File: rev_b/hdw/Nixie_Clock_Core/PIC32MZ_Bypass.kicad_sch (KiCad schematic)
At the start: 18 parts

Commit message: lots of rev B control board schematic progress
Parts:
- renumbered C1616 to C?, C1622 to C?, C1601 to C?, C1615 to C?, C1608 to C?, C1609 to C?, C1602 to C?, C1623 to C?, L1601 to L?, L1602 to L?

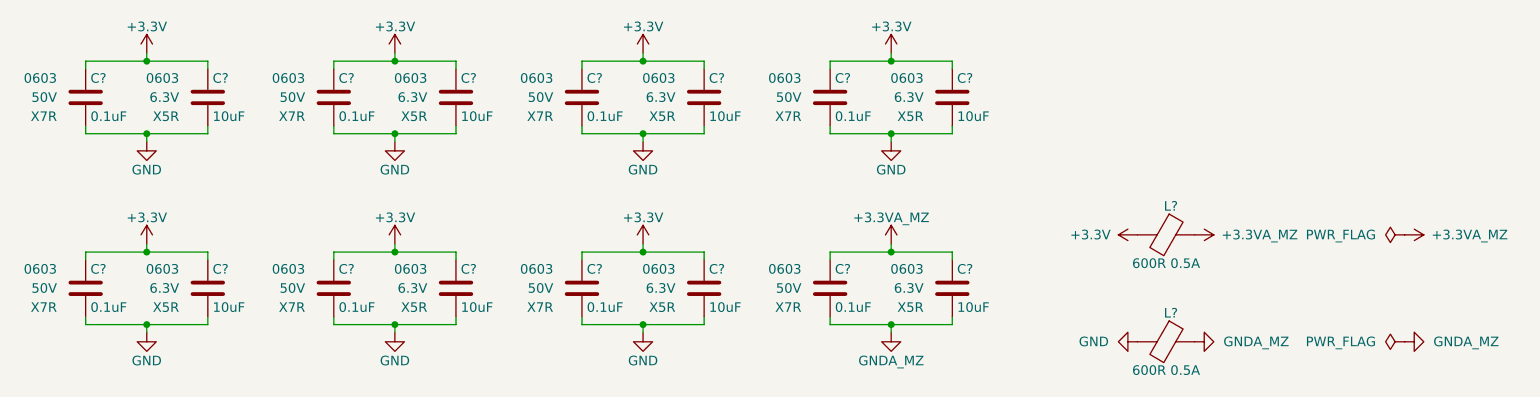
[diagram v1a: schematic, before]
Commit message: updated footprints, ran some DRC
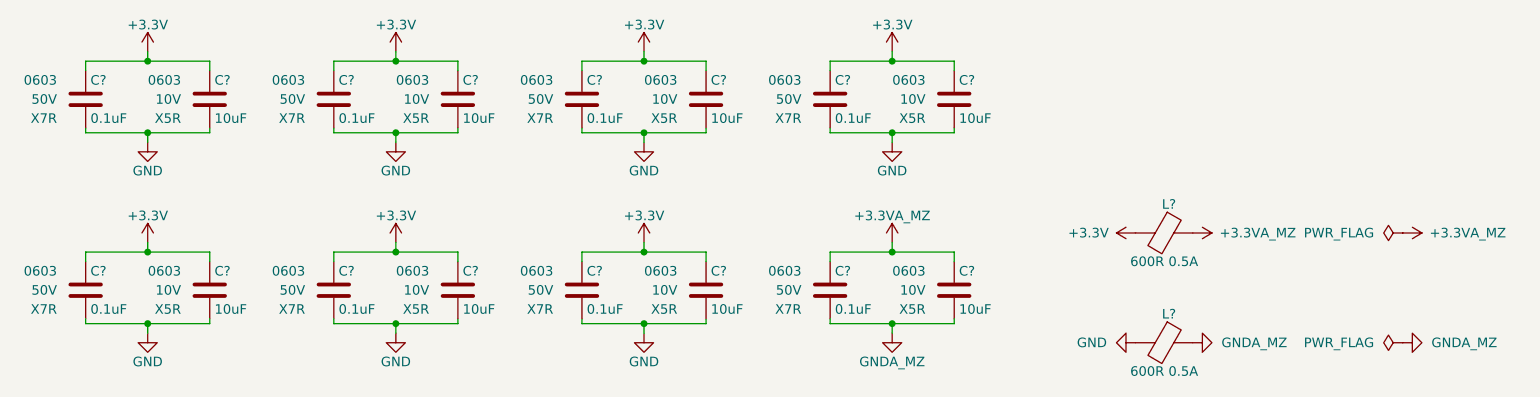
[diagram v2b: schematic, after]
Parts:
- C? (x8): Digi-Key PN 399-6856-1-ND -> (none)
- C? (x8): Digi-Key PN 490-12538-1-ND -> (none); Voltage 6.3V -> 10V
- L? (x2): Digi-Key PN 732-2389-1-ND -> (none)

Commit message: hid all passive refdes on core PCB
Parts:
- C? (x8): Digi-Key PN (none) -> 1276-1935-1-ND
- C? (x8): Digi-Key PN (none) -> 1276-1871-1-ND
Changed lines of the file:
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@@
       (effects (font (size 1.27 1.27)) (justify right))
     )
-    (property "Digi-Key PN" "" (at 13.716 275.082 0)
+    (property "Digi-Key PN" "1276-1935-1-ND" (at 13.716 275.082 0)
       (effects (font (size 1.27 1.27)) hide)
     )
@@
       (effects (font (size 1.27 1.27)) (justify right))
     )
-    (property "Digi-Key PN" "" (at 46.736 249.682 0)
+    (property "Digi-Key PN" "1276-1935-1-ND" (at 46.736 249.682 0)
       (effects (font (size 1.27 1.27)) hide)
     )
@@
       (effects (font (size 1.27 1.27)) (justify right))
     )
-    (property "Digi-Key PN" "" (at -52.324 249.682 0)
+    (property "Digi-Key PN" "1276-1935-1-ND" (at -52.324 249.682 0)
       (effects (font (size 1.27 1.27)) hide)
     )
@@
       (effects (font (size 1.27 1.27)) (justify right))
     )
-    (property "Digi-Key PN" "" (at 13.716 249.682 0)
+    (property "Digi-Key PN" "1276-1935-1-ND" (at 13.716 249.682 0)
       (effects (font (size 1.27 1.27)) hide)
     )
@@
       (effects (font (size 1.27 1.27)) (justify right))
     )
-    (property "Digi-Key PN" "" (at 96.52 74.93 0)
+    (property "Digi-Key PN" "1276-1871-1-ND" (at 96.52 74.93 0)
       (effects (font (size 1.27 1.27)) hide)
     )
@@
       (effects (font (size 1.27 1.27)) (justify right))
     )
-    (property "Digi-Key PN" "" (at 162.56 74.93 0)
+    (property "Digi-Key PN" "1276-1871-1-ND" (at 162.56 74.93 0)
       (effects (font (size 1.27 1.27)) hide)
     )
@@
       (effects (font (size 1.27 1.27)) (justify right))
     )
-    (property "Digi-Key PN" "" (at 96.52 100.33 0)
+    (property "Digi-Key PN" "1276-1871-1-ND" (at 96.52 100.33 0)
       (effects (font (size 1.27 1.27)) hide)
     )
@@
       (effects (font (size 1.27 1.27)) (justify right))
     )
-    (property "Digi-Key PN" "" (at -19.304 249.682 0)
+    (property "Digi-Key PN" "1276-1935-1-ND" (at -19.304 249.682 0)
       (effects (font (size 1.27 1.27)) hide)
     )
@@
       (effects (font (size 1.27 1.27)) (justify right))
     )
-    (property "Digi-Key PN" "" (at 129.54 74.93 0)
+    (property "Digi-Key PN" "1276-1871-1-ND" (at 129.54 74.93 0)
       (effects (font (size 1.27 1.27)) hide)
     )
@@
       (effects (font (size 1.27 1.27)) (justify right))
     )
-    (property "Digi-Key PN" "" (at -19.304 275.082 0)
+    (property "Digi-Key PN" "1276-1935-1-ND" (at -19.304 275.082 0)
       (effects (font (size 1.27 1.27)) hide)
     )
@@
       (effects (font (size 1.27 1.27)) (justify right))
     )
-    (property "Digi-Key PN" "" (at -52.324 275.082 0)
+    (property "Digi-Key PN" "1276-1935-1-ND" (at -52.324 275.082 0)
       (effects (font (size 1.27 1.27)) hide)
     )
@@
       (effects (font (size 1.27 1.27)) (justify right))
     )
-    (property "Digi-Key PN" "" (at 63.5 100.33 0)
+    (property "Digi-Key PN" "1276-1871-1-ND" (at 63.5 100.33 0)
       (effects (font (size 1.27 1.27)) hide)
     )
@@
       (effects (font (size 1.27 1.27)) (justify right))
     )
-    (property "Digi-Key PN" "" (at 129.54 100.33 0)
+    (property "Digi-Key PN" "1276-1871-1-ND" (at 129.54 100.33 0)
       (effects (font (size 1.27 1.27)) hide)
     )
@@
       (effects (font (size 1.27 1.27)) (justify right))
     )
-    (property "Digi-Key PN" "" (at 162.56 100.33 0)
+    (property "Digi-Key PN" "1276-1871-1-ND" (at 162.56 100.33 0)
       (effects (font (size 1.27 1.27)) hide)
     )
@@
       (effects (font (size 1.27 1.27)) (justify right))
     )
-    (property "Digi-Key PN" "" (at 63.5 74.93 0)
+    (property "Digi-Key PN" "1276-1871-1-ND" (at 63.5 74.93 0)
       (effects (font (size 1.27 1.27)) hide)
     )
@@
       (effects (font (size 1.27 1.27)) (justify right))
     )
-    (property "Digi-Key PN" "" (at 46.736 275.082 0)
-      (effects (font (size 1.27 1.27)) hide)
-    )
+    (property "Digi-Key PN" "1276-1935-1-ND" (at 46.736 275.082 0)
+      (effects (font (size 1.27 1.27)) hide)
+    )

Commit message: added BOM
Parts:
- L? (x2): Digi-Key PN (none) -> 490-1014-1-ND
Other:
- title: (none) -> Nixie Clock Redux Core Board
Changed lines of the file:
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@@
   (paper "A")
   (title_block
-    (date "2023-05-12")
-    (rev "PRELIM")
+    (title "Nixie Clock Redux Core Board")
+    (date "2023-07-30")
+    (rev "B")
     (company "Drew Maatman")
   )
@@
       (effects (font (size 1.27 1.27)) hide)
     )
-    (property "Digi-Key PN" "" (at 94.996 -149.352 0)
+    (property "Digi-Key PN" "490-1014-1-ND" (at 94.996 -149.352 0)
       (effects (font (size 1.27 1.27)) hide)
     )
@@
       (effects (font (size 1.27 1.27)) hide)
     )
-    (property "Digi-Key PN" "" (at 94.996 -134.747 0)
-      (effects (font (size 1.27 1.27)) hide)
-    )
+    (property "Digi-Key PN" "490-1014-1-ND" (at 94.996 -134.747 0)
+      (effects (font (size 1.27 1.27)) hide)
+    )
